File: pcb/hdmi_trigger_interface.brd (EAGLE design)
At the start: 78.7 x 63.5 mm, 2 parts

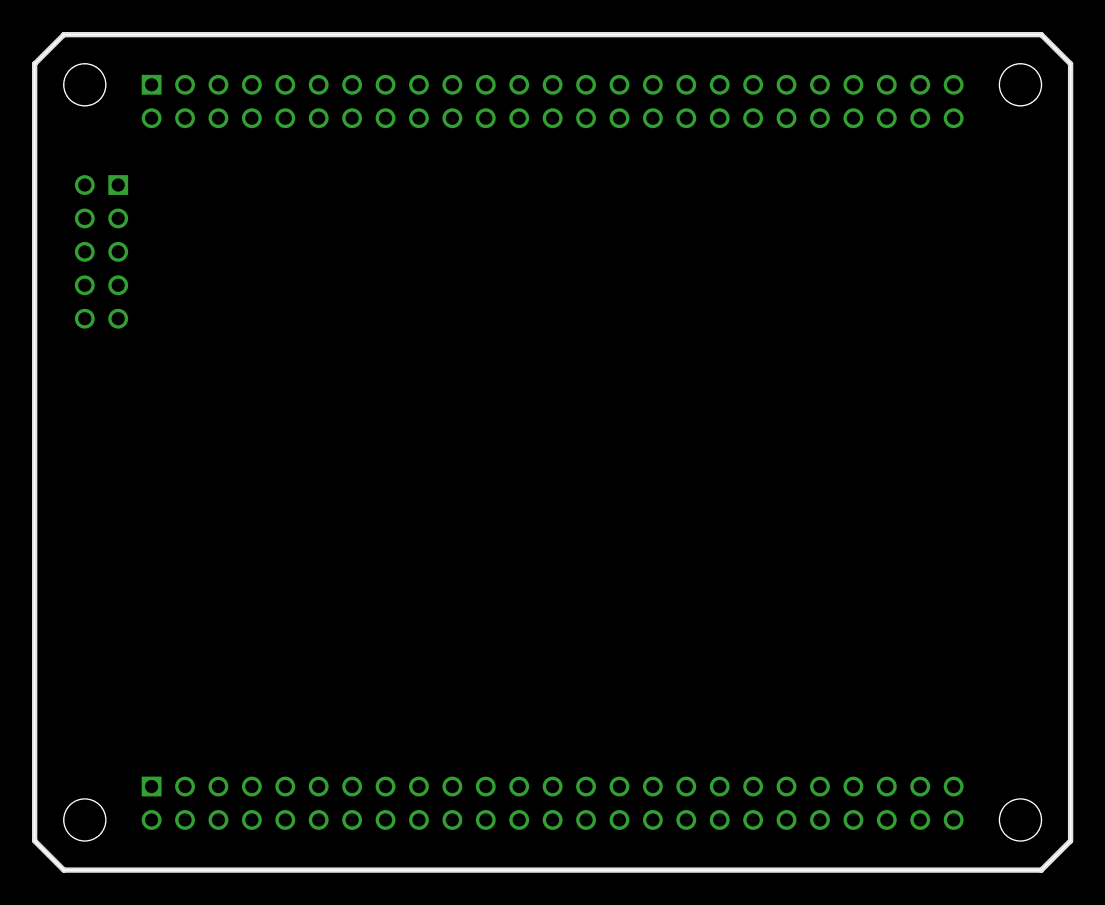
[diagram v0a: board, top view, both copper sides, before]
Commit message: work on hdmi integration into basler trigger circuitry
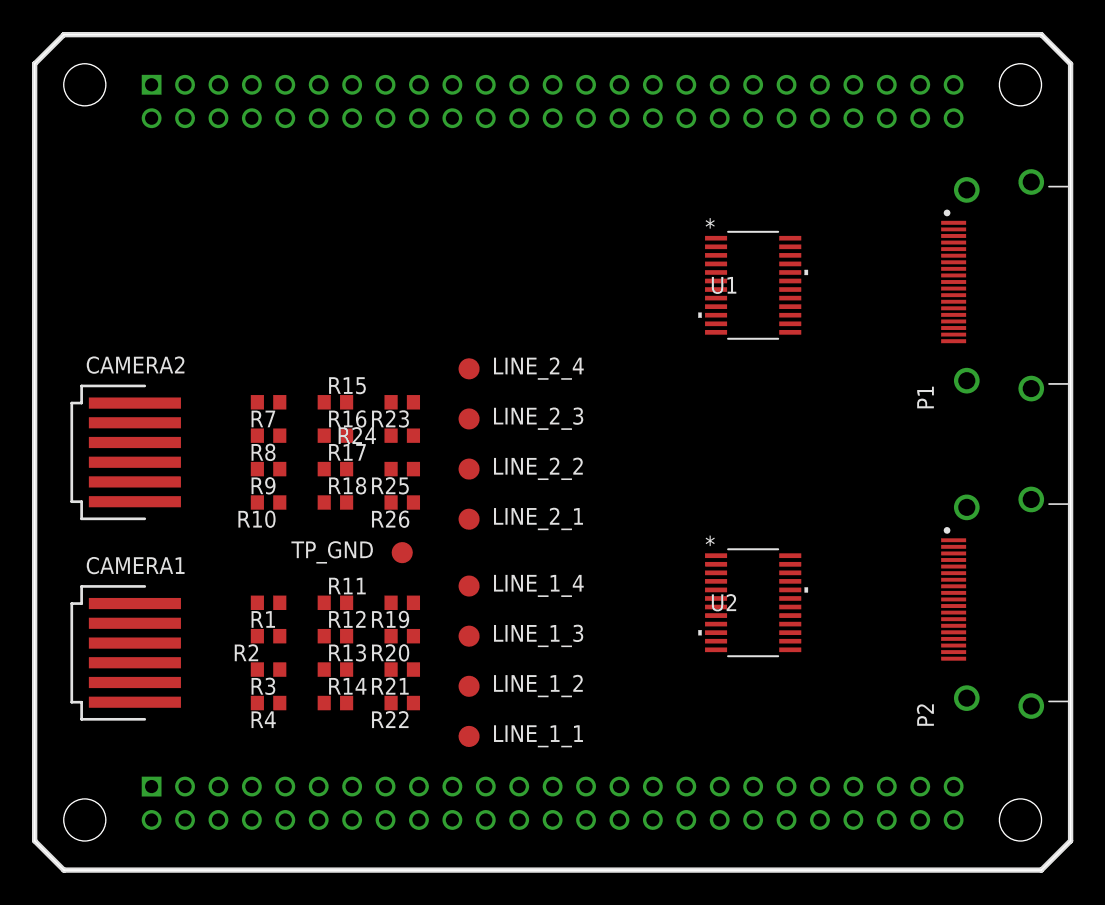
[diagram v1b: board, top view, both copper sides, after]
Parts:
- added CAMERA1, CAMERA2: 87438-06, con-molex:87438-06
- added LINE_1_1, LINE_1_2, LINE_1_3, LINE_1_4, LINE_2_1, LINE_2_2, LINE_2_3, LINE_2_4, TP_GND: TPTP16R, testpad:TP16R
- added P1, P2: 10029449-001RLF, 10029449-001RLF:FCI_10029449-001RLF
- added R1, R10, R11, R12, R13, R14, R15, R16, R17, R18, R19, R2, R20, R21, R22, R23, R24, R25, R26, R3, R4, R7, R8, R9: (no value), rcl:R0603
- added U1, U2: TPD12S016PWR, TPD12S016:PW24
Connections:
- new net 3V3: R11.2, R12.2, R13.2, R14.2, R15.2, R16.2, R17.2, R18.2, U$1.V@1, U$1.V@2
- new net CLK1_N: P1.12, U$1.143, U1.15
- new net CLK1_P: P1.10, U$1.144, U1.16
- new net CLK2_N: P2.12, U$1.120
- new net CLK2_P: P2.10, U$1.121
- new net D01_N: P1.9, U$1.141, U1.17
- new net D01_P: P1.7, U$1.142, U1.18
- new net D02_N: P2.9, U$1.118
- new net D02_P: P2.7, U$1.119
- new net D11_N: P1.6, U$1.139, U1.20
- new net D11_P: P1.4, U$1.140, U1.21
- new net D12_N: P2.6, U$1.116
- new net D12_P: P2.4, U$1.117
- new net D21_N: P1.3, U$1.137, U1.22
- new net D21_P: P1.1, U$1.138, U1.23
- new net D22_N: P2.3, U$1.114
- new net D22_P: P2.1, U$1.115
- new net GND: CAMERA1.5, CAMERA1.6, CAMERA2.5, CAMERA2.6, P1.11, P1.17, P1.2, P1.5, P1.8, P2.11, P2.17, P2.2, P2.5, P2.8, R19.1, R20.1, R21.1, R22.1, R23.1, R24.1, R25.1, R26.1, TP_GND.TP, U2.19
- new net GND@1: U$1.GND@1, U$1.GND@2, U$1.GND@3, U$1.GND@4
- new net GND_2: U1.6, U2.6
- new net GND_3: U2.14
- new net HP1: P1.19, U1.10
- new net HP2: P2.19
- new net LINE_1_1: LINE_1_1.TP, R14.1, R22.2, R4.1
- new net LINE_1_2: LINE_1_2.TP, R13.1, R21.2, R3.1
- new net LINE_1_3: LINE_1_3.TP, R12.1, R2.1, R20.2
- new net LINE_1_4: LINE_1_4.TP, R1.1, R11.1, R19.2
- new net LINE_2_1: LINE_2_1.TP, R10.1, R18.1, R26.2
- new net LINE_2_2: LINE_2_2.TP, R17.1, R25.2, R9.1
- new net LINE_2_3: LINE_2_3.TP, R16.1, R24.2, R8.1
- new net LINE_2_4: LINE_2_4.TP, R15.1, R23.2, R7.1
- new net N$1: U1.13
- new net N$10: CAMERA2.2, R8.2
- new net N$11: CAMERA2.3, R9.2
- new net N$12: CAMERA2.4, R10.2
- new net N$14: U1.19
- new net N$19: U1.14
- new net N$22: P1.18
- new net N$3: U1.24
- new net N$39: P2.18
- new net N$5: CAMERA1.1, R1.2
- new net N$6: CAMERA1.2, R2.2
- new net N$7: CAMERA1.3, R3.2
- new net N$8: CAMERA1.4, R4.2
- new net N$9: CAMERA2.1, R7.2
- new net SCL1: P1.15, U1.8
- new net SCL1_M: U$1.1, U1.2
- new net SCL2: P2.15, U$1.112
- new net SDA1: P1.16, U1.9
- new net SDA1_M: U$1.2, U1.3
- new net SDA2: P2.16, U$1.111
- new net VCC5V: U1.11, U2.11
- new net VCCA: U2.24

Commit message: almost done with routing
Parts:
- removed P1, P2: 10029449-001RLF, 10029449-001RLF:FCI_10029449-001RLF
- added C1: 0.1uF, rcl:C0603
- added C2: 1uF, rcl:C0603
- added HDMI_1, HDMI_2: 10029449-001RLF, 10029449-001RLF:FCI_10029449-001RLF
- added R5, R6: 3k, rcl:R0603
- added Y1: SI514, lupa300-components:XTAL-6PIN
- moved LINE_1_1 18.5 mm to (15.2, 15.2)
- moved LINE_1_2 18.2 mm to (15.2, 17.8)
- moved LINE_2_1 18.2 mm to (15.2, 30.5)
- moved LINE_1_3 18.0 mm to (15.2, 20.3)
- moved LINE_2_2 18.0 mm to (15.2, 33.0)
- moved LINE_1_4 17.8 mm to (15.2, 22.9)
- moved LINE_2_3 17.8 mm to (15.2, 35.6)
- moved LINE_2_4 17.8 mm to (15.2, 38.1)
- moved TP_GND 13.0 mm to (15.2, 26.7)
- moved U2 7.65 mm to (62.2, 21.0)
- moved R14 4.58 mm to (25.4, 16.5)
- moved R4 4.58 mm to (20.3, 16.5)
- moved R13 4.58 mm to (25.4, 19.1)
- moved R3 4.58 mm to (20.3, 19.1)
- moved R1 4.58 mm to (20.3, 24.1)
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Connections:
- removed net GND@1: U$1.GND@1, U$1.GND@2, U$1.GND@3, U$1.GND@4
- removed net GND_2: U1.6, U2.6
- removed net GND_3: U2.14
- removed net N$1: U1.13
- removed net N$14: U1.19
- removed net N$19: U1.14
- removed net N$22: P1.18
- removed net N$3: U1.24
- removed net N$39: P2.18
- removed net VCC5V: U1.11, U2.11
- removed net VCCA: U2.24
- new net 5V: U$1.RAW@1, U$1.RAW@2, U1.11, U2.11
- new net 5VHDMI1: HDMI_1.18, U1.13
- new net 5VHDMI2: HDMI_2.18, U2.13
- new net CTHPD1: U1.12
- new net CTHPD2: U2.12
- new net HP1_M: U1.4, U1.5
- new net HP2_M: U2.4, U2.5
- new net PROG_CLK: U$1.51, Y1.P$4
- new net SCL2_M: U$1.112, U2.2
- new net SCL_C: R5.1, U$1.23, Y1.P$2
- new net SDA2_M: U$1.111, U2.3
- new net SDA_C: R6.1, U$1.24, Y1.P$1
- net 3V3: now also C1.1, C2.1, R5.2, R6.2, U1.24, U2.24, Y1.P$6
- net CLK1_N: now also HDMI_1.12; no longer P1.12
- net CLK1_P: now also HDMI_1.10; no longer P1.10
- net CLK2_N: now also HDMI_2.12, U2.15; no longer P2.12
- net CLK2_P: now also HDMI_2.10, U2.16; no longer P2.10
- net D01_N: now also HDMI_1.9; no longer P1.9
- net D01_P: now also HDMI_1.7; no longer P1.7
- net D02_N: now also HDMI_2.9, U2.17; no longer P2.9
- net D02_P: now also HDMI_2.7, U2.18; no longer P2.7
- net D11_N: now also HDMI_1.6; no longer P1.6
- net D11_P: now also HDMI_1.4; no longer P1.4
- net D12_N: now also HDMI_2.6, U2.20; no longer P2.6
- net D12_P: now also HDMI_2.4, U2.21; no longer P2.4
- net D21_N: now also HDMI_1.3; no longer P1.3
- net D21_P: now also HDMI_1.1; no longer P1.1
- net D22_N: now also HDMI_2.3, U2.22; no longer P2.3
- net D22_P: now also HDMI_2.1, U2.23; no longer P2.1
- net GND: now also C1.2, C2.2, HDMI_1.11, HDMI_1.17, HDMI_1.2, HDMI_1.5, HDMI_1.8, HDMI_2.11, HDMI_2.17, HDMI_2.2, HDMI_2.5, HDMI_2.8, U$1.GND@1, U$1.GND@2, U$1.GND@3, U$1.GND@4, U$1.GND@6, U1.14, U1.19, U1.6, U2.14, U2.6, Y1.P$3; no longer P1.11, P1.17, P1.2, P1.5, P1.8, P2.11, P2.17, P2.2, P2.5, P2.8
- net HP1: now also HDMI_1.19; no longer P1.19
- net HP2: now also HDMI_2.19, U2.10; no longer P2.19
- net LINE_1_1: now also U$1.12; no longer LINE_1_1.TP
- net LINE_1_2: now also U$1.11; no longer LINE_1_2.TP
- net LINE_1_3: now also U$1.15; no longer LINE_1_3.TP
- net LINE_1_4: now also U$1.14; no longer LINE_1_4.TP
- net LINE_2_1: now also U$1.17; no longer LINE_2_1.TP
- net LINE_2_2: now also U$1.16; no longer LINE_2_2.TP
- net LINE_2_3: now also U$1.22; no longer LINE_2_3.TP
- net LINE_2_4: now also U$1.21; no longer LINE_2_4.TP
- net N$10: now also LINE_2_3.TP
- net N$11: now also LINE_2_2.TP
- net N$12: now also LINE_2_1.TP
- net N$5: now also LINE_1_4.TP
- net N$6: now also LINE_1_3.TP
- net N$7: now also LINE_1_2.TP
- net N$8: now also LINE_1_1.TP
- net N$9: now also LINE_2_4.TP
- net SCL1: now also HDMI_1.15; no longer P1.15
- net SCL2: now also HDMI_2.15, U2.8; no longer P2.15, U$1.112
- net SDA1: now also HDMI_1.16; no longer P1.16
- net SDA2: now also HDMI_2.16, U2.9; no longer P2.16, U$1.111
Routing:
- net 3V3: track 0.00 -> 176.4 mm, vias 0 -> 12
- net 5V: track 0.00 -> 166.4 mm
- net GND: track 0.00 -> 79.2 mm, vias 0 -> 23
- net LINE_1_1: track 0.00 -> 63.5 mm
- net LINE_1_3: track 0.00 -> 57.3 mm
- net LINE_1_2: track 0.00 -> 57.3 mm
- net LINE_1_4: track 0.00 -> 50.5 mm
- net D22_P: track 0.00 -> 46.5 mm
- net LINE_2_1: track 0.00 -> 46.1 mm
- net D22_N: track 0.00 -> 45.8 mm
- net D12_P: track 0.00 -> 45.2 mm
- net D12_N: track 0.00 -> 44.8 mm
- net D02_P: track 0.00 -> 44.8 mm
- net D02_N: track 0.00 -> 44.0 mm
- net CLK2_P: track 0.00 -> 43.3 mm
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- added copper zone on layer 1, net 3V3
- added copper zone on layer 16, net 3V3
- added copper zone on layer 16, net GND
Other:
- board text added: "3v3 Pull Up"
- board text added: "Camera IO Config"
- board text added: "Dual HDMI + MojoV3 + Basler Dr. Daniel L. Lau Matt Ruffner Ying Yu University of Kentucky 2019"
- board text added: "For 0603 series resistor, cut trace then place"
- board text added: "Pull Down"

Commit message: board layout 90% done, need parts list then will order
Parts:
- added C10, C3, C4, C5, C6, C7, C8, C9: 1uF, rcl:C0603
- added R27, R28, R29, R30: 10k, rcl:R0603
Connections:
- new net N$13: C9.1, HDMI_1.P1, HDMI_1.P2, HDMI_1.P3, HDMI_1.P4, R29.1
- new net N$14: C10.1, HDMI_2.P1, HDMI_2.P2, HDMI_2.P3, HDMI_2.P4, R30.1
- net 3V3: now also C7.1, C8.1, R27.1, R28.1
- net 5V: now also C3.1, C5.1
- net 5VHDMI1: now also C4.1
- net 5VHDMI2: now also C6.1
- net CTHPD1: now also R27.2, U$1.7
- net CTHPD2: now also R28.2, U$1.102
- net GND: now also C10.2, C3.2, C4.2, C5.2, C6.2, C7.2, C8.2, C9.2, R29.2, R30.2
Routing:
- net CTHPD2: track 0.00 -> 46.9 mm
- net CTHPD1: track 0.00 -> 21.9 mm
- net 3V3: track 176.4 -> 198.0 mm, vias 12 -> 14
- net GND: track 79.2 -> 93.8 mm, vias 23 -> 34
- net N$13: track 0.00 -> 6.33 mm
- net N$14: track 0.00 -> 5.76 mm
- net 5V: track 166.4 -> 170.8 mm
- net SCL2: track 12.7 -> 15.9 mm
- net SDA2: track 12.6 -> 15.7 mm
- net HP2: track 12.0 -> 14.1 mm
- net 5VHDMI1: track 13.7 -> 15.4 mm
- net 5VHDMI2: track 5.40 -> 6.92 mm
- net D12_P: track 45.2 -> 46.2 mm
- net D12_N: track 44.8 -> 45.8 mm
- net CLK2_N: track 42.3 -> 43.3 mm
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
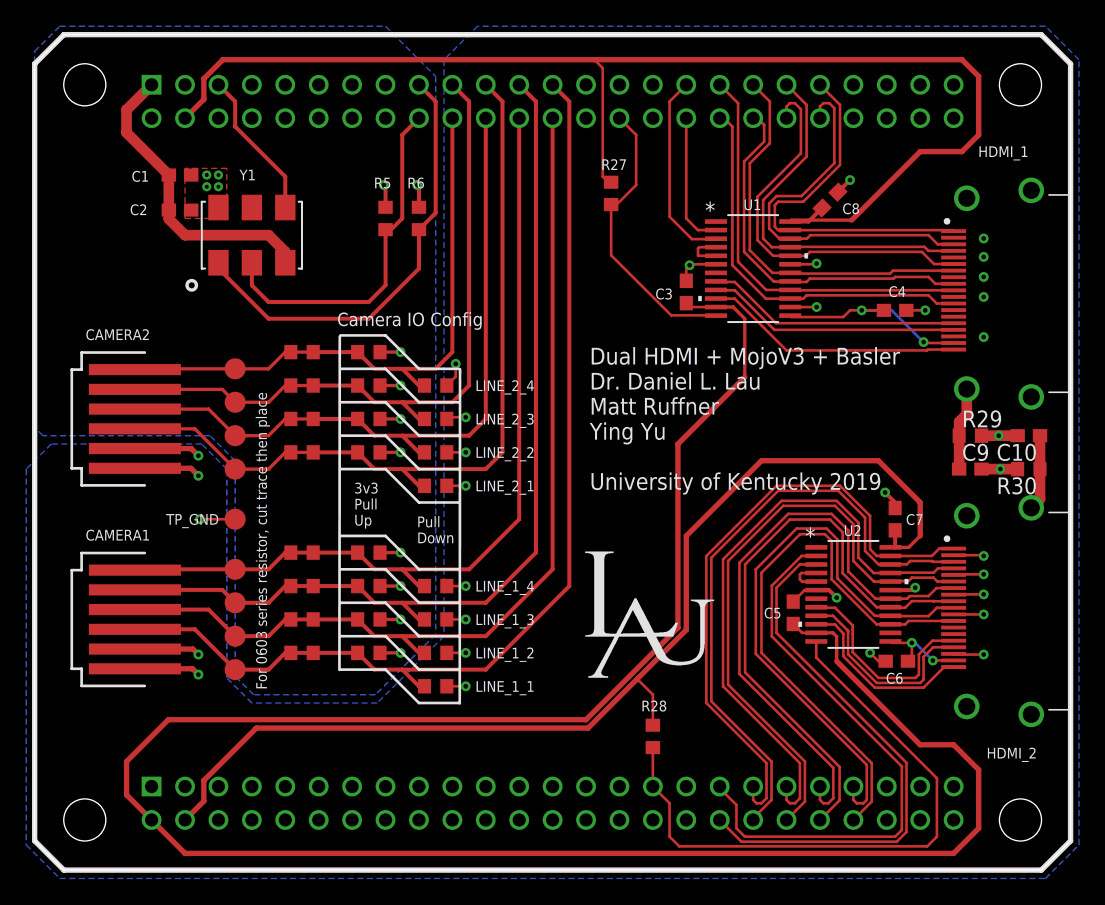
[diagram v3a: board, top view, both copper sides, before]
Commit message: added images from manufacturing render and gerbers sent to pcbway
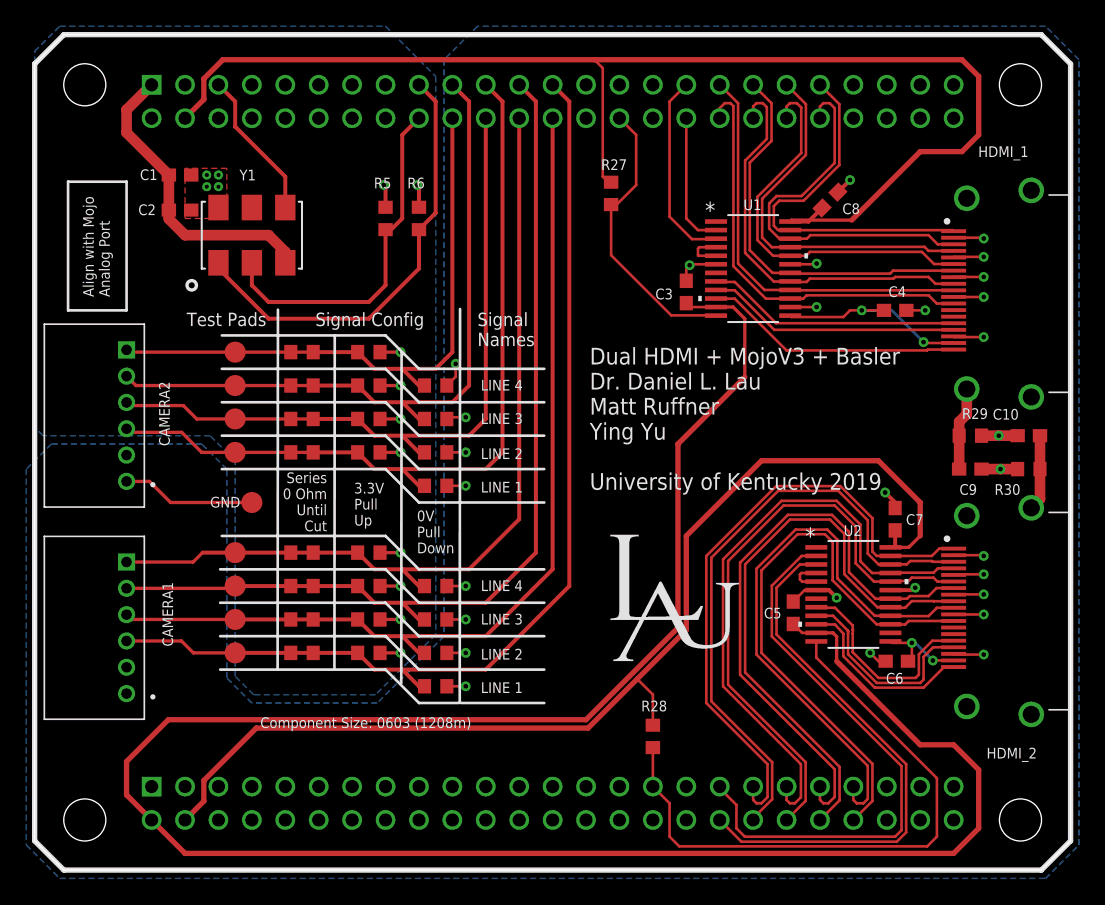
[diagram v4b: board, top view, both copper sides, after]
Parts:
- removed LINE_2_4: TPTP16R, testpad:TP16R
- added LINE_4: LINE_1, testpad:TP16R
- CAMERA1, CAMERA2: value 87438-06 -> S6B-PH-K-S(LF)(SN); device con-molex:87438-06 -> S6B-PH-K-S_LF__SN_:JST_S6B-PH-K-S(LF)(SN)
- LINE_2_1: value TPTP16R -> LINE_1
- LINE_2_2: value TPTP16R -> LINE_2
- LINE_2_3: value TPTP16R -> LINE_3
- moved TP_GND 1.80 mm to (16.5, 27.9)
- moved LINE_1_1 1.27 mm to (15.2, 16.5)
- moved LINE_1_2 1.27 mm to (15.2, 19.1)
- moved LINE_1_3 1.27 mm to (15.2, 21.6)
- moved LINE_1_4 1.27 mm to (15.2, 24.1)
- moved LINE_2_1 1.27 mm to (15.2, 31.8)
- moved LINE_2_2 1.27 mm to (15.2, 34.3)
- moved LINE_2_3 1.27 mm to (15.2, 36.8)
- moved CAMERA1 0.90 mm to (6.99, 18.4), turned to 270 degrees
- moved CAMERA2 0.68 mm to (6.99, 34.5), turned to 270 degrees
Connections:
- net N$9: now also LINE_4.TP; no longer LINE_2_4.TP
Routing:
- net D01_N: track 28.6 -> 31.1 mm
- net CLK1_N: track 30.0 -> 32.4 mm
- net GND: track 93.8 -> 92.7 mm, vias 34 -> 29
- net N$8: track 13.6 -> 12.9 mm
- net N$7: track 13.2 -> 12.6 mm
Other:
- board text added: "0V Pull Down"
- board text added: "3.3V Pull Up"
- board text added: "Align with Mojo Analog Port"
- board text added: "Basler Pinout Reference"
- board text added: "Component Size: 0603 (1208m)"
- board text added: "GND"
- board text added: "LINE 1"
- board text added: "LINE 2"
- board text added: "LINE 3"
- board text added: "LINE 4"
- board text added: "PIN 1 -> LINE 3 PIN 2 -> LINE 1 PIN 3 -> LINE 4 PIN 4 -> LINE 2 PIN 5 -> GND PIN 6 -> GND"
- board text added: "Series 0 Ohm Until Cut"
- board text added: "Signal Config"
- board text added: "Signal Names"
- board text added: "Test Pads"
- board text removed: "3v3 Pull Up"
- board text removed: "Camera IO Config"
- board text removed: "For 0603 series resistor, cut trace then place"
- board text removed: "Pull Down"

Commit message: rerouting with a 4 layer board and 7.6mil traces and 6mil spacing for 100 ohm differential impedance' g
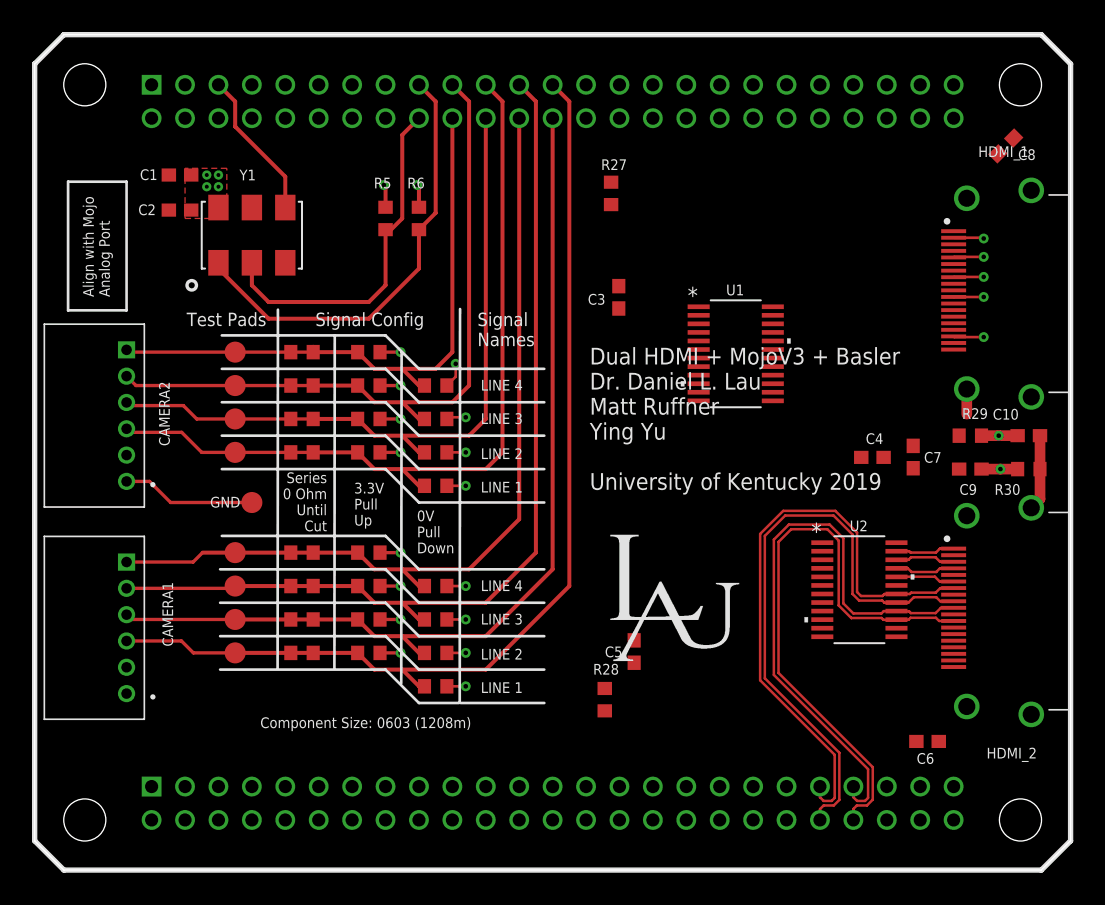
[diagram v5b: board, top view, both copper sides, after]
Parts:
- moved C8 14.0 mm to (73.8, 55.0)
- moved C5 12.4 mm to (45.6, 16.6)
- moved C4 11.3 mm to (63.7, 31.4)
- moved U1 6.61 mm to (53.3, 39.2)
- moved C6 6.53 mm to (67.9, 9.78)
- moved C3 5.15 mm to (44.4, 43.5)
- moved C7 4.92 mm to (66.8, 31.4)
- moved R28 4.60 mm to (43.3, 13.0)
- moved U2 0.58 mm to (62.7, 21.3)
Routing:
- net 3V3: track 198.0 -> 16.0 mm
- net 5V: track 170.8 -> 0.00 mm
- net GND: track 92.7 -> 39.2 mm, vias 29 -> 15
- net CTHPD2: track 46.9 -> 0.00 mm
- net SCL2_M: track 43.7 -> 0.00 mm
- net D22_P: track 47.6 -> 4.51 mm
- net D22_N: track 46.9 -> 4.56 mm
- net D12_P: track 46.4 -> 4.60 mm
- net SDA2_M: track 41.6 -> 0.00 mm
- net D12_N: track 45.9 -> 4.50 mm
- net CLK1_N: track 32.4 -> 0.00 mm
- net CLK1_P: track 31.4 -> 0.01 mm
- net D01_N: track 31.1 -> 0.00 mm
- net D01_P: track 30.2 -> 0.00 mm
- net D11_N: track 29.6 -> 0.00 mm
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- added copper zone on layer 15, net 3V3
- added copper zone on layer 2, net GND
- removed copper zone on layer 16, net 3V3
- removed copper zone on layer 16, net GND

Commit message: more routing
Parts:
- moved C5 12.9 mm to (57.9, 20.3)
- moved C6 4.80 mm to (67.7, 14.6), turned to 270 degrees
- moved C7 4.33 mm to (65.5, 27.3)
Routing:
- net D22_P: track 4.51 -> 41.5 mm
- net D22_N: track 4.56 -> 41.5 mm
- net D12_N: track 4.50 -> 41.1 mm
- net D12_P: track 4.60 -> 41.1 mm
- net D02_N: track 45.7 -> 40.8 mm
- net D02_P: track 45.6 -> 40.8 mm
- net CLK2_P: track 44.9 -> 40.8 mm
- net CLK2_N: track 44.8 -> 40.7 mm
